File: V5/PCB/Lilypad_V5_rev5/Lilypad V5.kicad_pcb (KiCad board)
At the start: 2 copper layers, 46.3 x 51.3 mm, 61 parts, among them J1 USB-C, J2 TRRS, Q1 AO3401A, SW1 BTN_RESET, SW2 BTN_USER, SW3 BTN_BOOT, U1 SRV05-4, U2 BQ21040, U3 M3406, U4 SRV05-4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

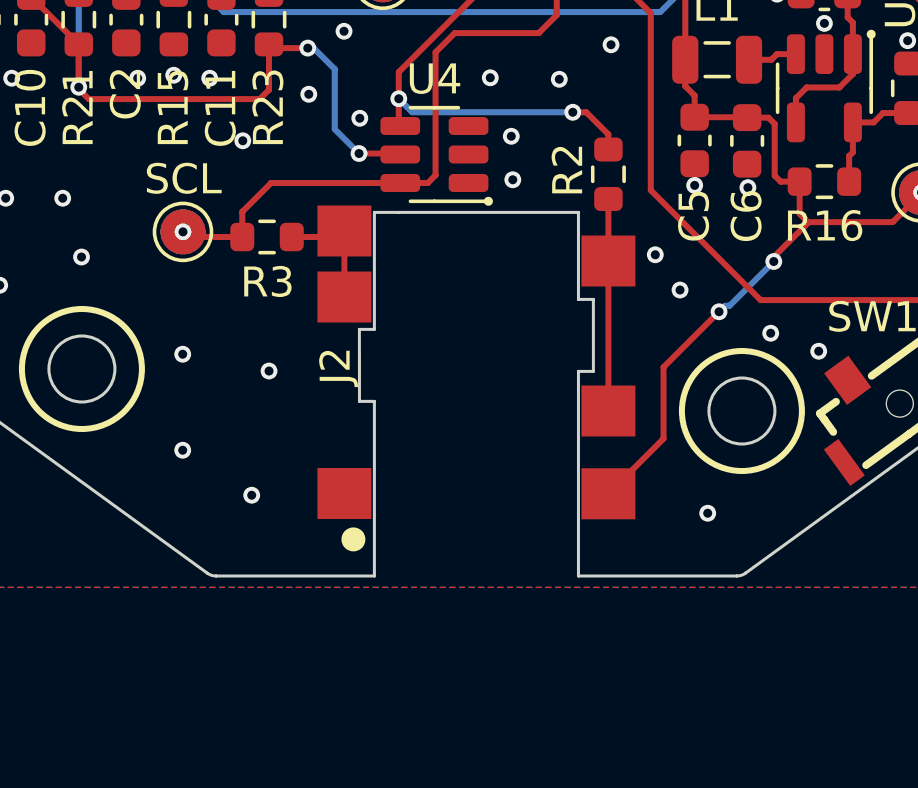
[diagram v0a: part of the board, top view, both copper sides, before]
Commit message: Model Updates, PCB Fixes
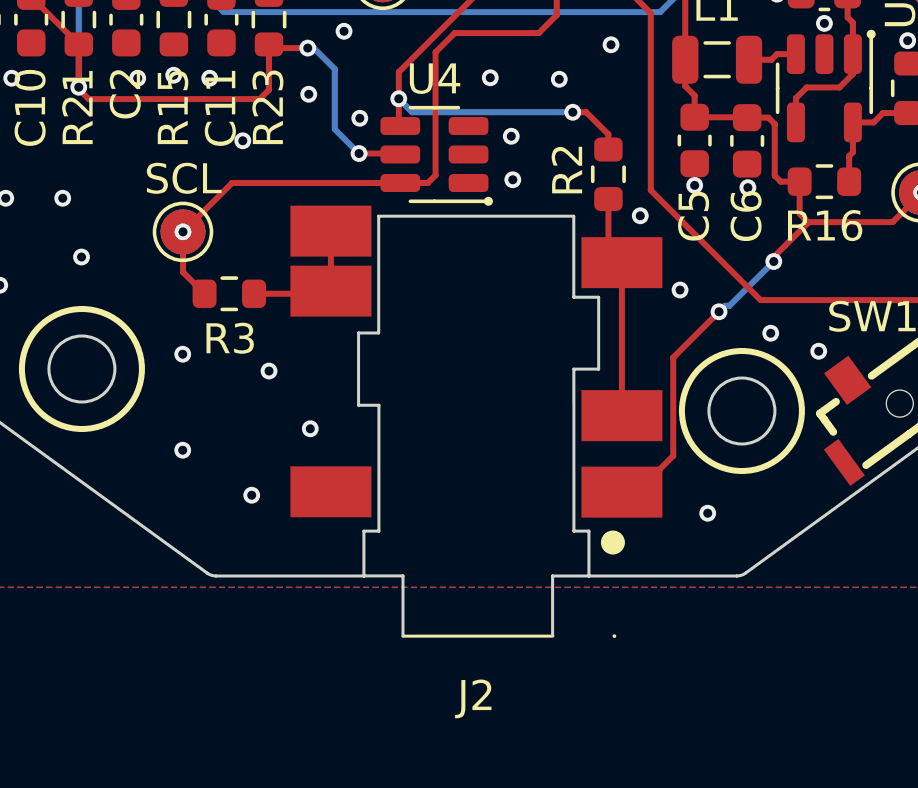
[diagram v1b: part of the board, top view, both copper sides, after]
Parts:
- J2: footprint Lilypad Footprints:AUDIO-SMD_PJ-342C -> Lilypad Footprints:AUDIO-SMD_PJ-342C-1
- moved R3 2.27 mm to (115.9, 117.2)
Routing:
- net SCL: track 38.3 -> 40.3 mm
- net Net-(J2-Pin_4): track 4.04 -> 4.88 mm
- net GND: vias 108 -> 109
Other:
- outline, holes or cut-outs redrawn
